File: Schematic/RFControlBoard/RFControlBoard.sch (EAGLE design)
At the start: 22 parts, among them IC1 LM320LZ-XX, U1 ATMEGA328P-PU

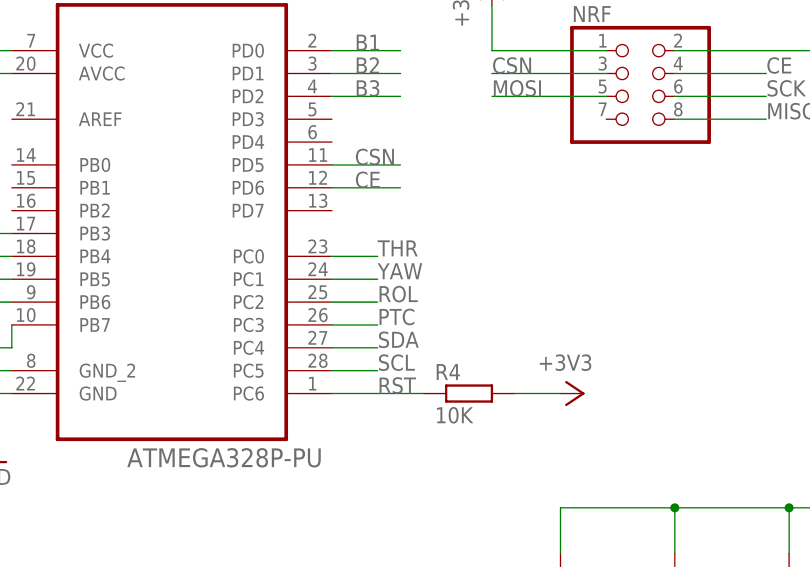
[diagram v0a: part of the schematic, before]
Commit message: Разведено для однослойной платы + пары проводков.
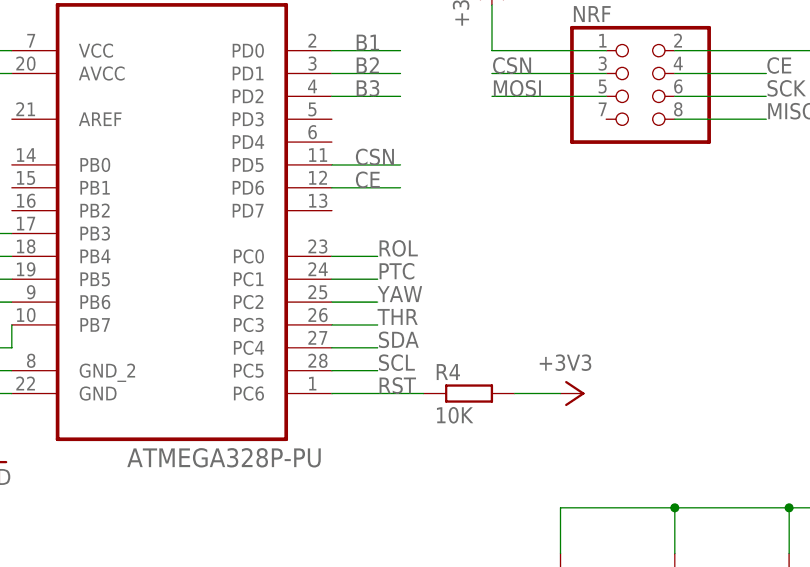
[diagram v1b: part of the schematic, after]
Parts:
- PWR: device pinhead:PINHD-1X2/90 -> pinhead:PINHD-1X2
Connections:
- net PTC: now also U1.PC1; no longer U1.PC3
- net ROL: now also U1.PC0; no longer U1.PC2
- net THR: now also U1.PC3; no longer U1.PC0
- net YAW: now also U1.PC2; no longer U1.PC1
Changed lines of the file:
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@@
 <part name="B1" library="pinhead" deviceset="PINHD-1X2" device=""/>
 <part name="ONOF" library="pinhead" deviceset="PINHD-1X2" device=""/>
-<part name="PWR" library="pinhead" deviceset="PINHD-1X2" device="/90"/>
 <part name="NRF" library="pinhead" deviceset="PINHD-2X4" device=""/>
 <part name="PIND" library="pinhead" deviceset="PINHD-1X2" device=""/>
@@
 <part name="GND7" library="supply1" deviceset="GND" device=""/>
 <part name="+3V7" library="supply1" deviceset="+3V3" device=""/>
+<part name="PWR" library="pinhead" deviceset="PINHD-1X2" device=""/>
 </parts>
 <sheets>
@@
 <instance part="B1" gate="G$1" x="172.72" y="-10.16"/>
 <instance part="ONOF" gate="G$1" x="12.7" y="66.04"/>
-<instance part="PWR" gate="G$1" x="-2.54" y="78.74" rot="R90"/>
 <instance part="NRF" gate="A" x="152.4" y="68.58"/>
 <instance part="PIND" gate="G$1" x="2.54" y="48.26" rot="MR270"/>
@@
 <instance part="GND7" gate="1" x="241.3" y="63.5"/>
 <instance part="+3V7" gate="G$1" x="241.3" y="88.9"/>
+<instance part="PWR" gate="G$1" x="-2.54" y="78.74" rot="R90"/>
 </instances>
 <busses>
@@
 <wire x1="0" y1="33.02" x2="0" y2="27.94" width="0.1524" layer="91"/>
 <wire x1="0" y1="50.8" x2="0" y2="66.04" width="0.1524" layer="91"/>
-<pinref part="PWR" gate="G$1" pin="1"/>
 <wire x1="0" y1="66.04" x2="-5.08" y2="66.04" width="0.1524" layer="91"/>
 <wire x1="-5.08" y1="66.04" x2="-5.08" y2="76.2" width="0.1524" layer="91"/>
@@
 <junction x="0" y="33.02"/>
 <junction x="20.32" y="33.02"/>
+<pinref part="PWR" gate="G$1" pin="1"/>
 </segment>
 <segment>
@@
 <net name="N$1" class="0">
 <segment>
-<pinref part="PWR" gate="G$1" pin="2"/>
 <wire x1="-2.54" y1="76.2" x2="-2.54" y2="68.58" width="0.1524" layer="91"/>
 <pinref part="ONOF" gate="G$1" pin="1"/>
 <wire x1="-2.54" y1="68.58" x2="10.16" y2="68.58" width="0.1524" layer="91"/>
+<pinref part="PWR" gate="G$1" pin="2"/>
 </segment>
 </net>
@@
 </segment>
 <segment>
+<pinref part="U1" gate="A" pin="PC3"/>
+<wire x1="119.38" y1="43.18" x2="124.46" y2="43.18" width="0.1524" layer="91"/>
+<label x="124.46" y="43.18" size="1.778" layer="95"/>
+</segment>
+</net>
+<net name="YAW" class="0">
+<segment>
+<pinref part="YAW" gate="A" pin="2"/>
+<wire x1="68.58" y1="0" x2="58.42" y2="0" width="0.1524" layer="91"/>
+<label x="58.42" y="0" size="1.778" layer="95"/>
+</segment>
+<segment>
+<pinref part="U1" gate="A" pin="PC2"/>
+<wire x1="119.38" y1="45.72" x2="124.46" y2="45.72" width="0.1524" layer="91"/>
+<label x="124.46" y="45.72" size="1.778" layer="95"/>
+</segment>
+</net>
+<net name="PTC" class="0">
+<segment>
+<pinref part="PTC" gate="A" pin="2"/>
+<wire x1="86.36" y1="0" x2="76.2" y2="0" width="0.1524" layer="91"/>
+<label x="76.2" y="0" size="1.778" layer="95"/>
+</segment>
+<segment>
+<pinref part="U1" gate="A" pin="PC1"/>
+<wire x1="119.38" y1="48.26" x2="124.46" y2="48.26" width="0.1524" layer="91"/>
+<label x="124.46" y="48.26" size="1.778" layer="95"/>
+</segment>
+</net>
+<net name="ROL" class="0">
+<segment>
+<pinref part="ROL" gate="A" pin="2"/>
+<wire x1="104.14" y1="0" x2="93.98" y2="0" width="0.1524" layer="91"/>
+<label x="93.98" y="0" size="1.778" layer="95"/>
+</segment>
+<segment>
 <pinref part="U1" gate="A" pin="PC0"/>
 <wire x1="119.38" y1="50.8" x2="124.46" y2="50.8" width="0.1524" layer="91"/>
@@
 </segment>
 </net>
-<net name="YAW" class="0">
-<segment>
-<pinref part="YAW" gate="A" pin="2"/>
-<wire x1="68.58" y1="0" x2="58.42" y2="0" width="0.1524" layer="91"/>
-<label x="58.42" y="0" size="1.778" layer="95"/>
-</segment>
-<segment>
-<pinref part="U1" gate="A" pin="PC1"/>
-<wire x1="119.38" y1="48.26" x2="124.46" y2="48.26" width="0.1524" layer="91"/>
-<label x="124.46" y="48.26" size="1.778" layer="95"/>
-</segment>
-</net>
-<net name="PTC" class="0">
-<segment>
-<pinref part="PTC" gate="A" pin="2"/>
-<wire x1="86.36" y1="0" x2="76.2" y2="0" width="0.1524" layer="91"/>
-<label x="76.2" y="0" size="1.778" layer="95"/>
-</segment>
-<segment>
-<pinref part="U1" gate="A" pin="PC3"/>
-<wire x1="119.38" y1="43.18" x2="124.46" y2="43.18" width="0.1524" layer="91"/>
-<label x="124.46" y="43.18" size="1.778" layer="95"/>
-</segment>
-</net>
-<net name="ROL" class="0">
-<segment>
-<pinref part="ROL" gate="A" pin="2"/>
-<wire x1="104.14" y1="0" x2="93.98" y2="0" width="0.1524" layer="91"/>
-<label x="93.98" y="0" size="1.778" layer="95"/>
-</segment>
-<segment>
-<pinref part="U1" gate="A" pin="PC2"/>
-<wire x1="119.38" y1="45.72" x2="124.46" y2="45.72" width="0.1524" layer="91"/>
-<label x="124.46" y="45.72" size="1.778" layer="95"/>
-</segment>
-</net>

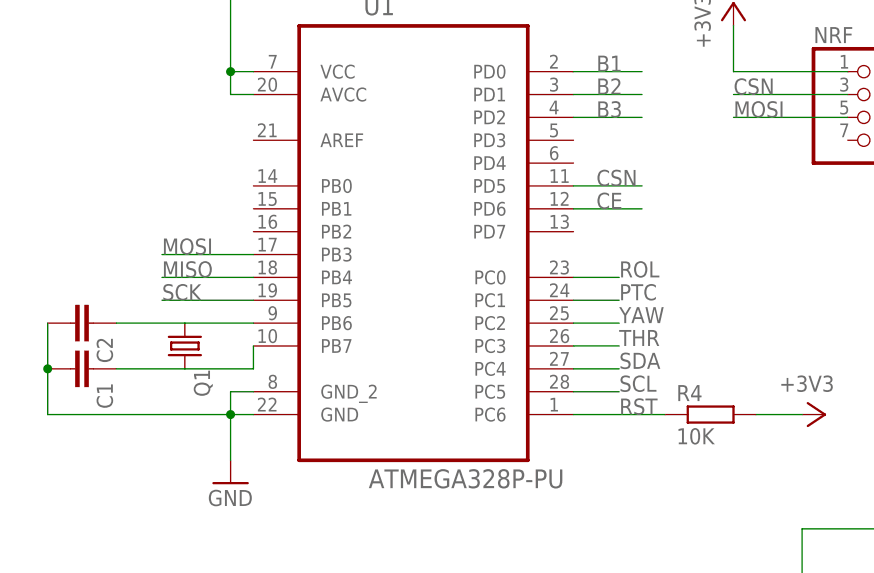
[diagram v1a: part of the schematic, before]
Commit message: RC Control board (RCCB): 1) Schematic is updated for laser ironing PCB production :) 2) Initial version of RCCB firmware (3.3v 8Mhz). not tested.
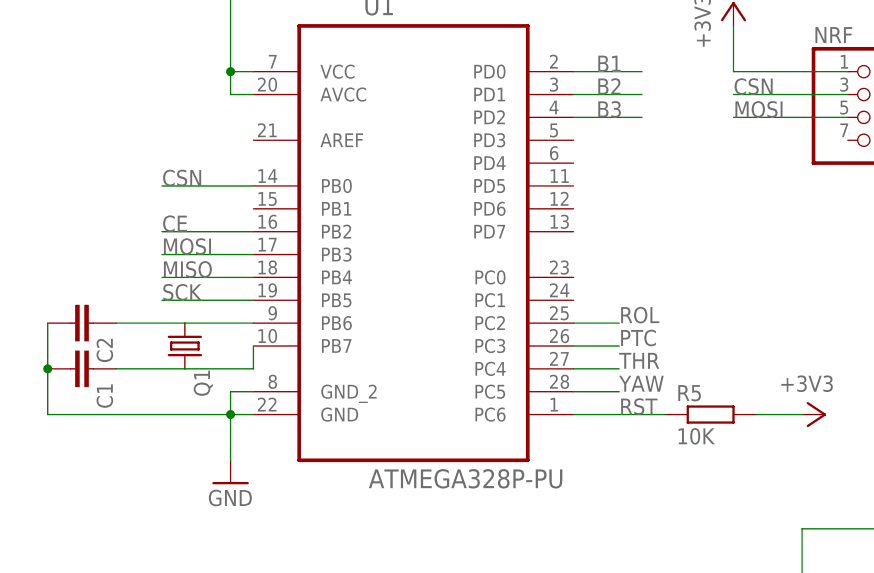
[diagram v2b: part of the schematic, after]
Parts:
- removed R4: 10K, rcl:R-EU_0207/10
- added R5: 10K, rcl:R-EU_0207/15
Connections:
- removed net SCL: U1.PC5
- removed net SDA: U1.PC4
- net +3V3: now also R5.2; no longer R4.2
- net CE: now also U1.PB2; no longer U1.PD6
- net CSN: now also U1.PB0; no longer U1.PD5
- net PTC: now also U1.PC3; no longer U1.PC1
- net ROL: now also U1.PC2; no longer U1.PC0
- net RST: now also R5.1; no longer R4.1
- net THR: now also U1.PC4; no longer U1.PC3
- net YAW: now also U1.PC5; no longer U1.PC2
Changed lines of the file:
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@@
 </variantdefs>
 <classes>
-<class number="0" name="default" width="0" drill="0">
+<class number="0" name="default" width="0.508" drill="0">
+</class>
+<class number="1" name="GND" width="2.286" drill="0">
 </class>
 </classes>
@@
 <part name="GND5" library="supply1" deviceset="GND" device=""/>
 <part name="+3V6" library="supply1" deviceset="+3V3" device=""/>
-<part name="R4" library="rcl" deviceset="R-EU_" device="0207/10" value="10K"/>
 <part name="GND7" library="supply1" deviceset="GND" device=""/>
 <part name="+3V7" library="supply1" deviceset="+3V3" device=""/>
 <part name="PWR" library="pinhead" deviceset="PINHD-1X2" device=""/>
+<part name="R5" library="rcl" deviceset="R-EU_" device="0207/15" value="10K"/>
 </parts>
 <sheets>
@@
 <instance part="GND5" gate="1" x="182.88" y="71.12"/>
 <instance part="+3V6" gate="G$1" x="137.16" y="81.28"/>
-<instance part="R4" gate="G$1" x="134.62" y="35.56"/>
 <instance part="GND7" gate="1" x="241.3" y="63.5"/>
 <instance part="+3V7" gate="G$1" x="241.3" y="88.9"/>
 <instance part="PWR" gate="G$1" x="-2.54" y="78.74" rot="R90"/>
+<instance part="R5" gate="G$1" x="134.62" y="35.56"/>
 </instances>
 <busses>
@@
 <segment>
 <pinref part="+3V5" gate="G$1" pin="+3V3"/>
-<pinref part="R4" gate="G$1" pin="2"/>
 <wire x1="144.78" y1="35.56" x2="139.7" y2="35.56" width="0.1524" layer="91"/>
+<pinref part="R5" gate="G$1" pin="2"/>
 </segment>
 <segment>
@@
 </segment>
 <segment>
-<pinref part="U1" gate="A" pin="PD5"/>
-<wire x1="119.38" y1="60.96" x2="127" y2="60.96" width="0.1524" layer="91"/>
-<label x="121.92" y="60.96" size="1.778" layer="95"/>
+<pinref part="U1" gate="A" pin="PB0"/>
+<wire x1="83.82" y1="60.96" x2="73.66" y2="60.96" width="0.1524" layer="91"/>
+<label x="73.66" y="60.96" size="1.778" layer="95"/>
 </segment>
 </net>
@@
 </segment>
 <segment>
-<pinref part="U1" gate="A" pin="PD6"/>
-<wire x1="119.38" y1="58.42" x2="127" y2="58.42" width="0.1524" layer="91"/>
-<label x="121.92" y="58.42" size="1.778" layer="95"/>
+<pinref part="U1" gate="A" pin="PB2"/>
+<wire x1="83.82" y1="55.88" x2="73.66" y2="55.88" width="0.1524" layer="91"/>
+<label x="73.66" y="55.88" size="1.778" layer="95"/>
 </segment>
 </net>
@@
 </segment>
 <segment>
+<pinref part="U1" gate="A" pin="PC4"/>
+<wire x1="119.38" y1="40.64" x2="124.46" y2="40.64" width="0.1524" layer="91"/>
+<label x="124.46" y="40.64" size="1.778" layer="95"/>
+</segment>
+</net>
+<net name="YAW" class="0">
+<segment>
+<pinref part="YAW" gate="A" pin="2"/>
+<wire x1="68.58" y1="0" x2="58.42" y2="0" width="0.1524" layer="91"/>
+<label x="58.42" y="0" size="1.778" layer="95"/>
+</segment>
+<segment>
+<pinref part="U1" gate="A" pin="PC5"/>
+<wire x1="119.38" y1="38.1" x2="124.46" y2="38.1" width="0.1524" layer="91"/>
+<label x="124.46" y="38.1" size="1.778" layer="95"/>
+</segment>
+</net>
+<net name="PTC" class="0">
+<segment>
+<pinref part="PTC" gate="A" pin="2"/>
+<wire x1="86.36" y1="0" x2="76.2" y2="0" width="0.1524" layer="91"/>
+<label x="76.2" y="0" size="1.778" layer="95"/>
+</segment>
+<segment>
 <pinref part="U1" gate="A" pin="PC3"/>
 <wire x1="119.38" y1="43.18" x2="124.46" y2="43.18" width="0.1524" layer="91"/>
@@
 </segment>
 </net>
-<net name="YAW" class="0">
-<segment>
-<pinref part="YAW" gate="A" pin="2"/>
-<wire x1="68.58" y1="0" x2="58.42" y2="0" width="0.1524" layer="91"/>
-<label x="58.42" y="0" size="1.778" layer="95"/>
+<net name="ROL" class="0">
+<segment>
+<pinref part="ROL" gate="A" pin="2"/>
+<wire x1="104.14" y1="0" x2="93.98" y2="0" width="0.1524" layer="91"/>
+<label x="93.98" y="0" size="1.778" layer="95"/>
 </segment>
 <segment>
@@
 <wire x1="119.38" y1="45.72" x2="124.46" y2="45.72" width="0.1524" layer="91"/>
 <label x="124.46" y="45.72" size="1.778" layer="95"/>
-</segment>
-</net>
-<net name="PTC" class="0">
-<segment>
-<pinref part="PTC" gate="A" pin="2"/>
-<wire x1="86.36" y1="0" x2="76.2" y2="0" width="0.1524" layer="91"/>
-<label x="76.2" y="0" size="1.778" layer="95"/>
-</segment>
-<segment>
-<pinref part="U1" gate="A" pin="PC1"/>
-<wire x1="119.38" y1="48.26" x2="124.46" y2="48.26" width="0.1524" layer="91"/>
-<label x="124.46" y="48.26" size="1.778" layer="95"/>
-</segment>
-</net>
-<net name="ROL" class="0">
-<segment>
-<pinref part="ROL" gate="A" pin="2"/>
-<wire x1="104.14" y1="0" x2="93.98" y2="0" width="0.1524" layer="91"/>
-<label x="93.98" y="0" size="1.778" layer="95"/>
-</segment>
-<segment>
-<pinref part="U1" gate="A" pin="PC0"/>
-<wire x1="119.38" y1="50.8" x2="124.46" y2="50.8" width="0.1524" layer="91"/>
-<label x="124.46" y="50.8" size="1.778" layer="95"/>
 </segment>
 </net>
@@
 <segment>
 <pinref part="U1" gate="A" pin="PC6"/>
-<pinref part="R4" gate="G$1" pin="1"/>
 <wire x1="129.54" y1="35.56" x2="119.38" y2="35.56" width="0.1524" layer="91"/>
 <label x="124.46" y="35.56" size="1.778" layer="95"/>
+<pinref part="R5" gate="G$1" pin="1"/>
 </segment>
 <segment>
@@
 </segment>
 </net>
-<net name="SCL" class="0">
-<segment>
-<pinref part="U1" gate="A" pin="PC5"/>
-<wire x1="119.38" y1="38.1" x2="124.46" y2="38.1" width="0.1524" layer="91"/>
-<label x="124.46" y="38.1" size="1.778" layer="95"/>
-</segment>
-</net>
-<net name="SDA" class="0">
-<segment>
-<pinref part="U1" gate="A" pin="PC4"/>
-<wire x1="119.38" y1="40.64" x2="124.46" y2="40.64" width="0.1524" layer="91"/>
-<label x="124.46" y="40.64" size="1.778" layer="95"/>
-</segment>
-</net>

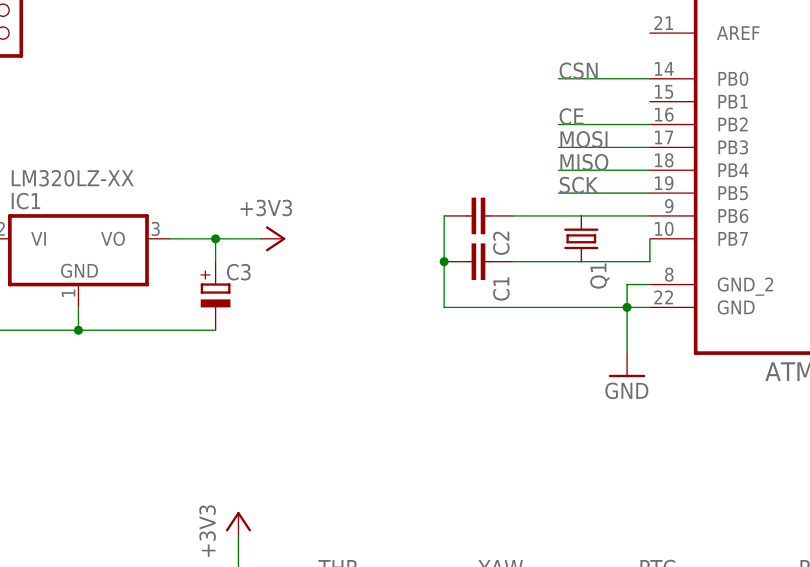
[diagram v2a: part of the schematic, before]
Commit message: Temporary disable acc control.
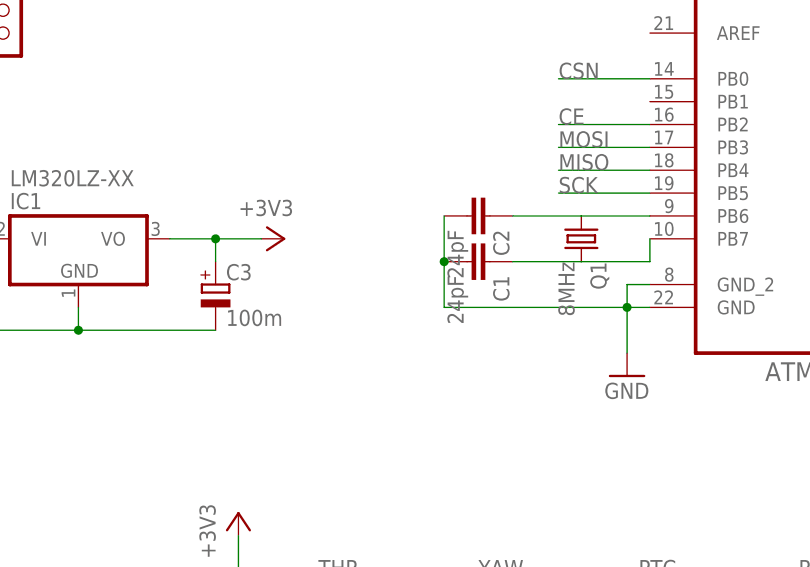
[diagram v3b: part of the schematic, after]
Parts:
- C1, C2: value (none) -> 24pF
- C3: value (none) -> 100m
- Q1: value (none) -> 8MHz
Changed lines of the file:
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@@
 <parts>
 <part name="U1" library="ATMEGA328" deviceset="ATMEGA328P-PU" device=""/>
-<part name="Q1" library="crystal" deviceset="CRYSTAL" device="HC49S"/>
-<part name="C1" library="capacitor-wima" deviceset="C" device="2,5-3"/>
-<part name="C2" library="capacitor-wima" deviceset="C" device="2,5-3"/>
+<part name="Q1" library="crystal" deviceset="CRYSTAL" device="HC49S" value="8MHz"/>
+<part name="C1" library="capacitor-wima" deviceset="C" device="2,5-3" value="24pF"/>
+<part name="C2" library="capacitor-wima" deviceset="C" device="2,5-3" value="24pF"/>
 <part name="THR" library="pinhead" deviceset="PINHD-1X3" device=""/>
 <part name="YAW" library="pinhead" deviceset="PINHD-1X3" device=""/>
@@
 <part name="GND3" library="supply1" deviceset="GND" device=""/>
 <part name="IC1" library="linear" deviceset="LM320LZ-XX" device=""/>
-<part name="C3" library="rcl" deviceset="CPOL-EU" device="E2.5-6"/>
+<part name="C3" library="rcl" deviceset="CPOL-EU" device="E2.5-6" value="100m"/>
 <part name="ISP" library="pinhead" deviceset="PINHD-2X3" device=""/>
 <part name="R1" library="rcl" deviceset="R-EU_" device="0207/10" value="10K"/>
